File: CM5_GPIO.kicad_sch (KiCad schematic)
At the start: 18 parts, among them J14 Micro_SD_Card_Det, J4 JST_SHBM04B-SRSS-TB, J5 THD-20-R, J9 RJMG201K21120FR, SW1 Right angle Tact button, SW2 SW_DIP_x04, U1 74LVC1G07SE-7, U3 RT9742GGJ5

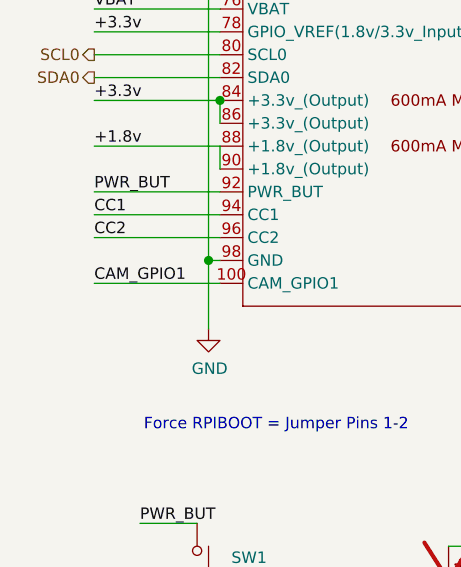
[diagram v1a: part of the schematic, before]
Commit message: change USB2.0
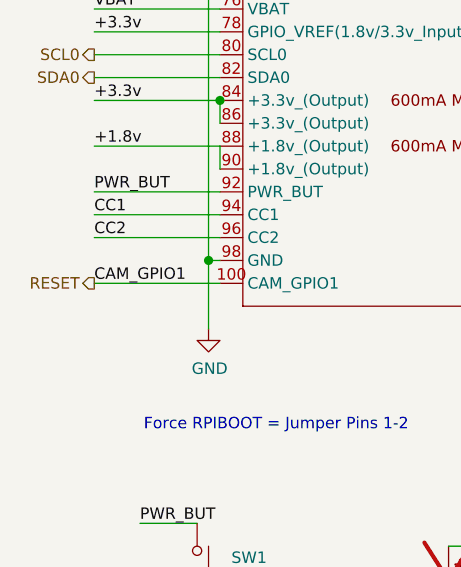
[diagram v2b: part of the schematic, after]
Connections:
- net CAM_GPIO1 renamed RESET

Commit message: end route
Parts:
- renumbered C135 to C108, J9 to J10, R16 to R18, R15 to R19
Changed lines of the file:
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@@
 		(dnp no)
 		(fields_autoplaced yes)
-		(property "Reference" "J9"
+		(property "Reference" "J10"
 			(at 257.81 126.9999 0)
 			(effects
@@
 			(project ""
 				(path "/dd07ab80-a59c-44f4-ac7d-849e21e1384e/92b565bf-b0e5-4fdf-876c-4b44381d5705"
-					(reference "J9")
+					(reference "J10")
 					(unit 1)
 				)
@@
 		(on_board yes)
 		(dnp no)
-		(property "Reference" "C135"
+		(property "Reference" "C108"
 			(at 197.231 102.9716 0)
 			(effects
@@
 			(project "mainboard4"
 				(path "/dd07ab80-a59c-44f4-ac7d-849e21e1384e/92b565bf-b0e5-4fdf-876c-4b44381d5705"
-					(reference "C135")
+					(reference "C108")
 					(unit 1)
 				)
@@
 		(on_board yes)
 		(dnp no)
-		(property "Reference" "R15"
+		(property "Reference" "R19"
 			(at 217.17 140.7922 90)
 			(effects
@@
 			(project "mainboard4"
 				(path "/dd07ab80-a59c-44f4-ac7d-849e21e1384e/92b565bf-b0e5-4fdf-876c-4b44381d5705"
-					(reference "R15")
+					(reference "R19")
 					(unit 1)
 				)
@@
 		(on_board yes)
 		(dnp no)
-		(property "Reference" "R16"
+		(property "Reference" "R18"
 			(at 217.17 133.1722 90)
 			(effects
@@
 			(project "mainboard4"
 				(path "/dd07ab80-a59c-44f4-ac7d-849e21e1384e/92b565bf-b0e5-4fdf-876c-4b44381d5705"
-					(reference "R16")
-					(unit 1)
-				)
+					(reference "R18")
+					(unit 1)
+				)

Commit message: fix screen
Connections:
- net +1.8v: no longer Module1.90 (+1.8v_(Output))

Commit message: データをアップロード
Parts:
- removed BT301: Battery_Cell, CM5IO:BatteryHolder_Keystone_3034_1x20mm, symbol Device:Battery_Cell
- removed C108: 100n, Capacitor_SMD:C_0402_1005Metric_Pad0.74x0.62mm_HandSolder, symbol Device:C
- removed C4: 10u, Capacitor_SMD:C_0805_2012Metric, symbol Device:C
- removed D2: LED Green, LED_SMD:LED_0603_1608Metric_Pad1.05x0.95mm_HandSolder, symbol Device:LED
- removed J10: RJMG201K21120FR, CM5IO:AMPHENOL_RJMG201K21120FR, symbol RJMG201K21120FR:RJMG201K21120FR
- removed Module1: Compute Module 5, CM5IO:Raspberry-Pi-5-Compute-Module, symbol CM5IO:ComputeModule5-CM5
- removed R18, R19: 470R, Resistor_SMD:R_0603_1608Metric_Pad0.98x0.95mm_HandSolder, symbol Device:R
- added C10: 10u, Capacitor_SMD:C_0805_2012Metric, symbol Device:C
- added C104, C105: 100n, Capacitor_SMD:C_0402_1005Metric_Pad0.74x0.62mm_HandSolder, symbol Device:C
- added D1: LED Green, LED_SMD:LED_0603_1608Metric_Pad1.05x0.95mm_HandSolder, symbol Device:LED
- added J11: 690-019-298-412, CM5IO:EDAC 690-019-298-412, symbol CM5IO:HDMI_A_1.4
- added J15: Conn_01x22_Female, CM5symbol:Hirose_FH12-22S-0.5SH_1x22-1MP_P0.50mm_Horizontal, symbol Connector:Conn_01x22_Socket
- added U16: RT9742SNGV, Package_TO_SOT_SMD:TSOT-23_HandSoldering, symbol CM5IO:RT9742SNGV
- renumbered D1 to D2, J4 to J6, SW2 to SW3
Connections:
- net +3.3V: now also D1.2 (A), J15.22 (Pin_22)
- net +5V: now also C104.1, U16.1 (IN)
- net GND: now also C10.2, C104.2, C105.2, J11.11 (CKS), J11.17 (GND), J11.2 (D2S), J11.5 (D1S), J11.8 (D0S), J11.SH1 (SH), J11.SH2 (SH), J11.SH3 (SH), J11.SH4 (SH), J15.1 (Pin_1), J15.10 (Pin_10), J15.13 (Pin_13), J15.16 (Pin_16), J15.19 (Pin_19), J15.4 (Pin_4), J15.7 (Pin_7), U16.3 (GND)
- net SD_PWR: now also C10.1
- net LED_nACT: now reaches R2.2
- net at R2.1: now also D1.1 (K)
- net +3.3v renamed 3.3V
- net PWR_BUT renamed POWER_SW
- net SD_PWR_ON renamed PWR_ON
- new net CEC: J11.13 (CEC)
- new net CKN: J11.12 (CK-)
- new net CKP: J11.10 (CK+)
- new net D0N: J11.9 (D0-)
- new net D0P: J11.7 (D0+)
- new net D1N: J11.6 (D1-)
- new net D1P: J11.4 (D1+)
- new net D2N: J11.3 (D2-)
- new net D2P: J11.1 (D2+)
- new net DSI0N: J15.2 (Pin_2)
- new net DSI0P: J15.3 (Pin_3)
- new net DSI1N: J15.5 (Pin_5)
- new net DSI1P: J15.6 (Pin_6)
- new net DSI2N: J15.11 (Pin_11)
- new net DSI2P: J15.12 (Pin_12)
- new net DSI3N: J15.14 (Pin_14)
- new net DSI3P: J15.15 (Pin_15)
- new net DSICN: J15.8 (Pin_8)
- new net DSICP: J15.9 (Pin_9)
- new net GPDI_5v: C105.1, J11.18 (+5V), U16.2 (OUT)
- new net GPIO0: J15.17 (Pin_17)
- new net GPIO1: J15.18 (Pin_18)
- new net HPD: J11.19 (HPD/HEAC-)
- new net SCL: J11.15 (SCL)
- new net SDA: J11.16 (SDA)
- new net TP_SCL: J15.20 (Pin_20)
- new net TP_SDA: J15.21 (Pin_21)
- no-connect marks 8 -> 4
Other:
- note added: "CONFIG"
- note added: "DSI/CSI Connectors"
- note added: "FAN"
- note added: "GDPI"
- note added: "LED"
- note added: "Switch"
- note removed: "Activity LED"
- note removed: "Ethernet"
- note removed: "FAN connector"
- note removed: "Not Fitted header"
- note removed: "PWR LED"
- moved on the sheet: D2, J14, J5, J6, R1, SW1, SW3, U1, U3
